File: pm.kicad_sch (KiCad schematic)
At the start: 15 parts, among them U10 INA237AIDGSR, U2 INA237AIDGSR, U6 INA237AIDGSR, U7 INA237AIDGSR, U9 INA237AIDGSR

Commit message: Added decouping caps
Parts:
- removed R25, R28, R29: 4.7K, symbol Device:R_US
- removed R26, R31, R32: SR: 0.001, symbol Device:R_US
- removed U10, U7, U9: INA237AIDGSR, VSSOP_IDGSR_TEX, symbol 2026-09-19_00-01-31:INA237AIDGSR
- added C40, C41: 0.1uF, symbol Device:C
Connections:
- net +3.3V: now also C40.1, C41.1
- net GND: now also C40.2, C41.2
- net +12V_B1 renamed +5.1V_UNFILT
- net +12V_B1_OUT renamed +5.1V
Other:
- note added: "5.1V Brick"
- note removed: "Brick 1"
- note removed: "Brick 2"
- note removed: "Brick 3"
- note removed: "Brick 4"
- note removed: "I2C Address: 0x42"
- note removed: "I2C Address: 0x43"
- note removed: "I2C Address: 0x44"

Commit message: Reverse polarity and power flow TBD, improved capacitance and labelling for nets
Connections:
- net +5.1V_UNFILT renamed +5.1V_RAW
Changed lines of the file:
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@@
 			)
 		)
-		(property "Value" "+5.1V_UNFILT"
+		(property "Value" "+5.1V_RAW"
 			(at 128.27 87.63 0)
 			(show_name no)

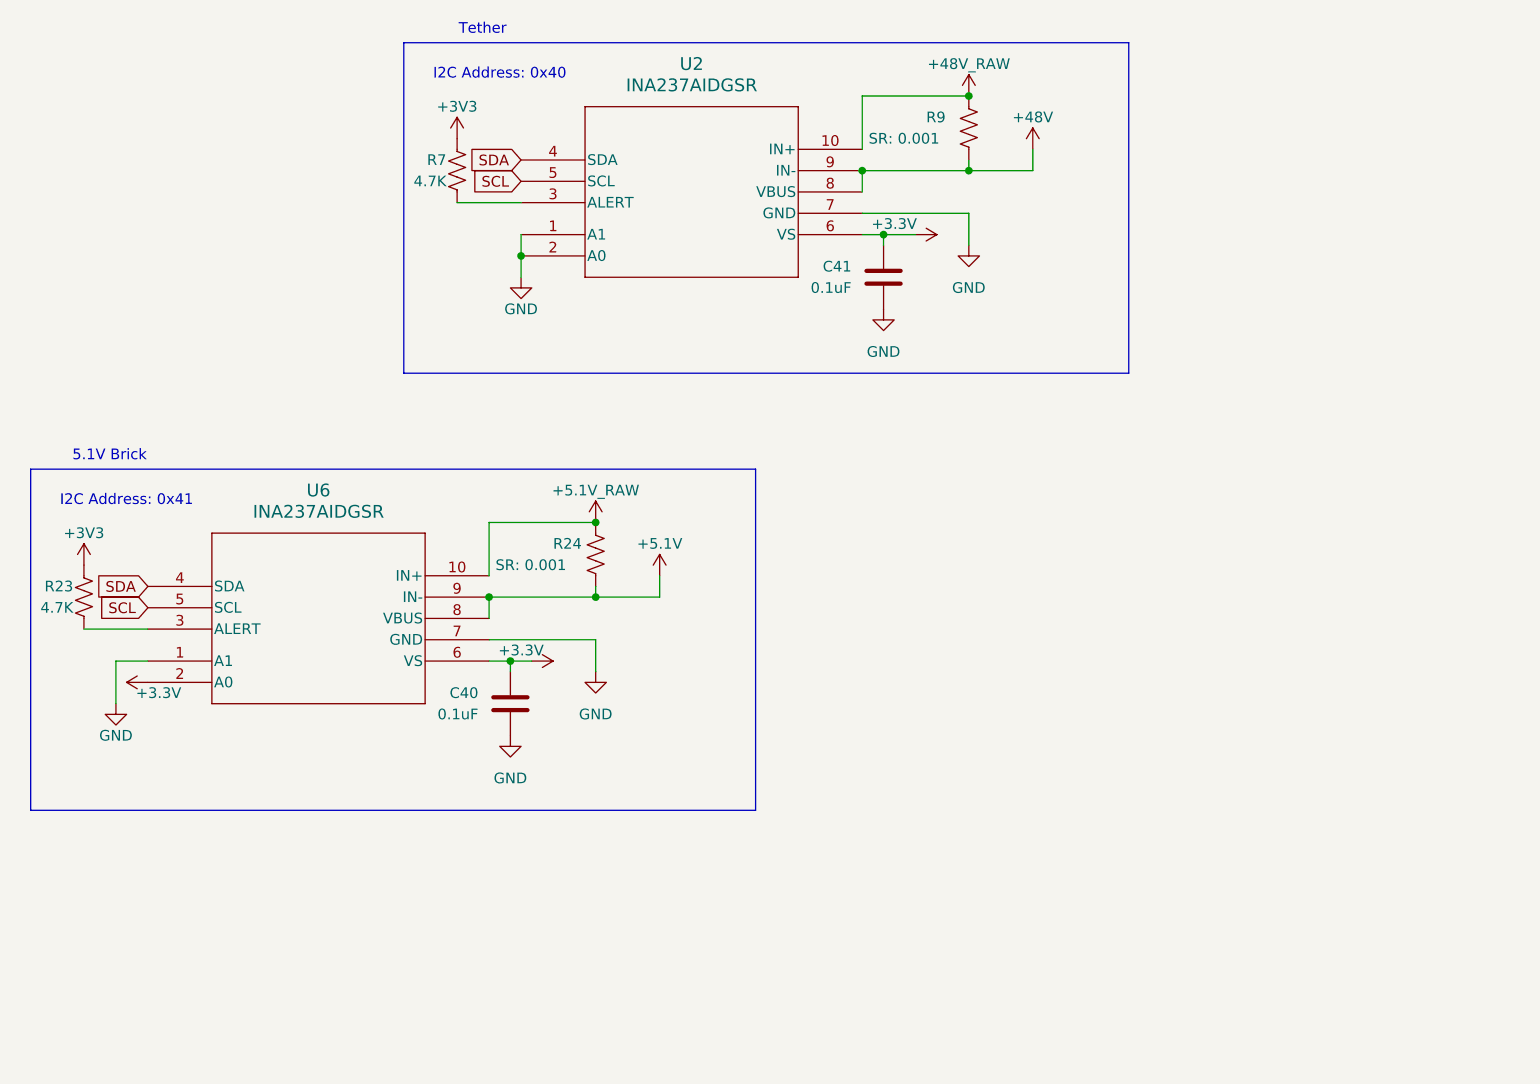
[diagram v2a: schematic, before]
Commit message: Prettified, more power changes and MCU pin changes and removing redundancies
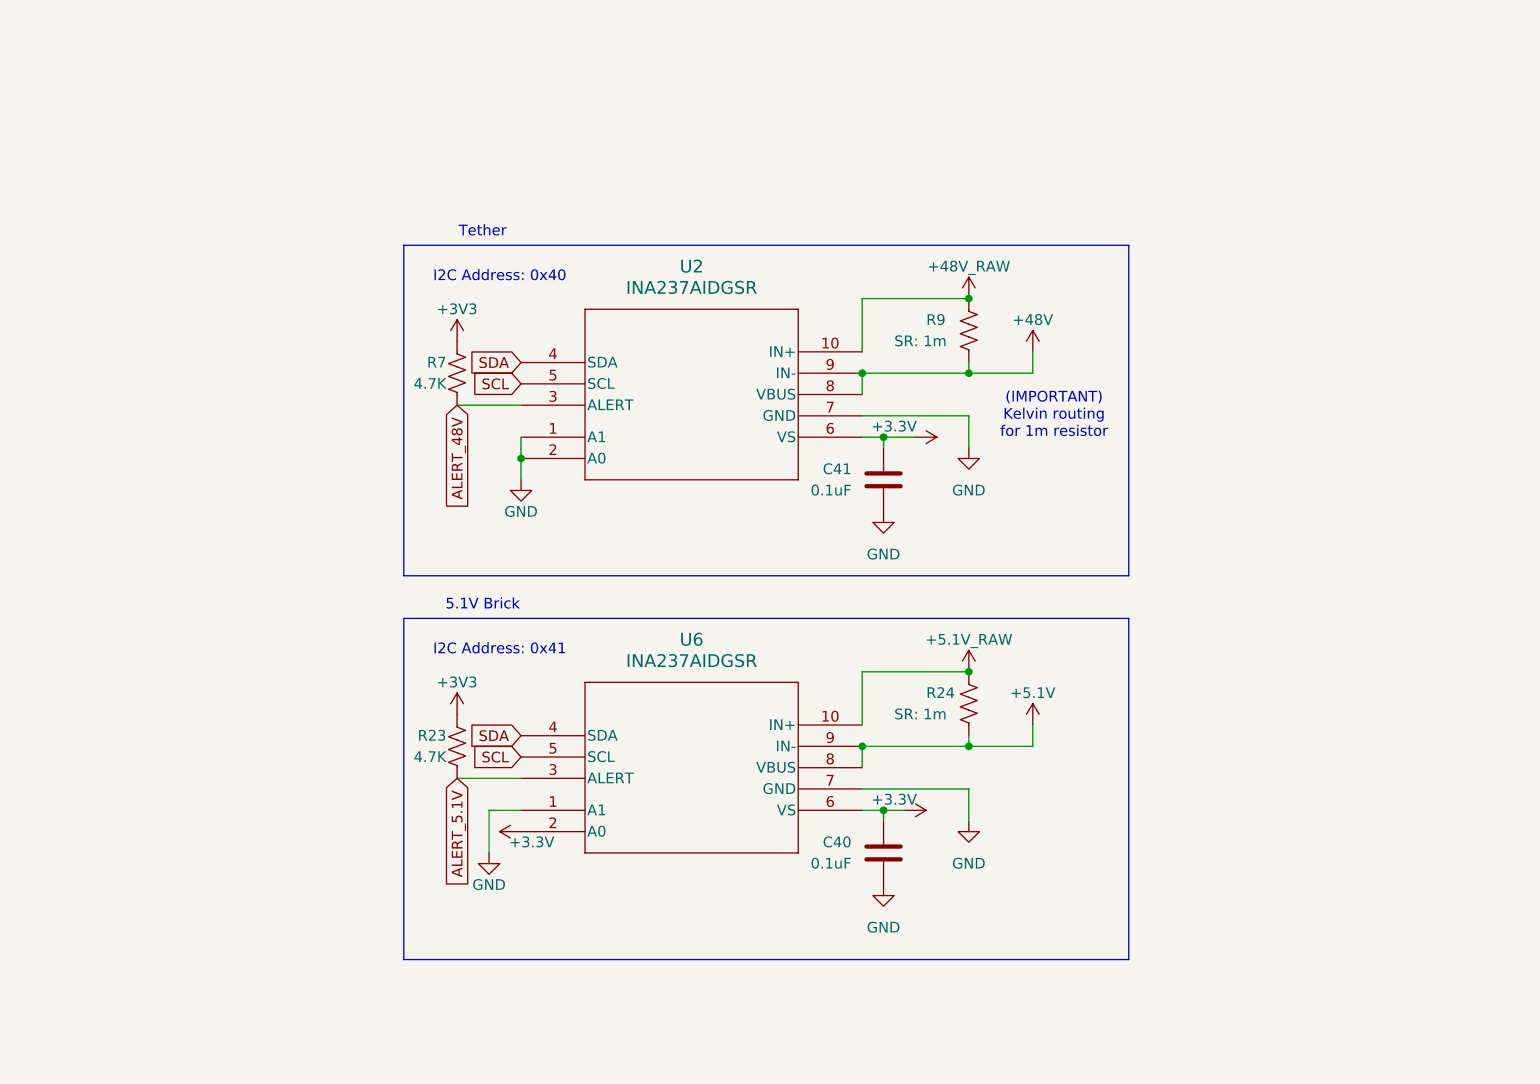
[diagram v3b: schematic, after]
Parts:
- R24, R9: value SR: 0.001 -> SR: 1m
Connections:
- net ALERT_5.1V: now reaches R23.2, U6.3 (ALERT)
- net ALERT_48V: now reaches R7.2, U2.3 (ALERT)
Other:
- note added: "(IMPORTANT) Kelvin routing for 1m resistor"
- moved on the sheet: C40, C41, R23, R24, R7, R9, U2, U6

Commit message: Replaced improper brick with new one
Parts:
- renumbered C41 to C42, C40 to C43, R7 to R21, R23 to R22, R9 to R23, U2 to U5
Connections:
- net ALERT_48V renamed INA_48V_ALERT_N
- net ALERT_5.1V renamed INA_5V1_ALERT_N
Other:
- note added: "(CHECKED)"
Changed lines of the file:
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@@
+		)
+	)
+	(text "(CHECKED)"
+		(exclude_from_sim no)
+		(at 125.73 101.6 0)
+		(effects
+			(font
+				(size 1.27 1.27)
+				(thickness 0.254)
+				(bold yes)
+				(color 224 48 15 1)
+			)
 		)
 	)
@@
 		)
 	)
+	(text "(CHECKED)"
+		(exclude_from_sim no)
+		(at 115.57 54.61 0)
+		(effects
+			(font
+				(size 1.27 1.27)
+				(thickness 0.254)
+				(bold yes)
+				(color 224 48 15 1)
+			)
+		)
+	)
 	(junction
 		(at 119.38 83.82)
@@
 		)
 	)
-	(global_label "ALERT_48V"
+	(global_label "INA_48V_ALERT_N"
 		(shape input)
 		(at 111.76 77.47 270)
@@
 		)
 		(property "Intersheetrefs" "${INTERSHEET_REFS}"
-			(at 111.76 90.4337 90)
+			(at 111.76 96.7233 90)
 			(hide yes)
 			(show_name no)
@@
 		)
 	)
-	(global_label "ALERT_5.1V"
+	(global_label "INA_5V1_ALERT_N"
 		(shape input)
 		(at 111.76 121.92 270)
@@
 		)
 		(property "Intersheetrefs" "${INTERSHEET_REFS}"
-			(at 111.76 135.4885 90)
+			(at 111.76 141.1733 90)
 			(hide yes)
 			(show_name no)
@@
 		(in_pos_files yes)
 		(dnp no)
-		(property "Reference" "R23"
+		(property "Reference" "R22"
 			(at 110.49 116.84 0)
 			(show_name no)
@@
 			(project "X19-Power-Slab-Board"
 				(path "/00000000-0000-0000-0000-000060e6118b/bbc862bf-048a-4900-acb1-a8352275c096"
-					(reference "R23")
+					(reference "R22")
 					(unit 1)
 				)
@@
 		(in_pos_files yes)
 		(dnp no)
-		(property "Reference" "#PWR032"
+		(property "Reference" "#PWR0105"
 			(at 119.38 92.71 0)
 			(hide yes)
@@
 			(project "X19-Power-Slab-Board"
 				(path "/00000000-0000-0000-0000-000060e6118b/bbc862bf-048a-4900-acb1-a8352275c096"
-					(reference "#PWR032")
+					(reference "#PWR0105")
 					(unit 1)
 				)
@@
 		(in_pos_files yes)
 		(dnp no)
-		(property "Reference" "#PWR0109"
+		(property "Reference" "#PWR0106"
 			(at 123.19 128.27 0)
 			(hide yes)
@@
 			(project "X19-Power-Slab-Board"
 				(path "/00000000-0000-0000-0000-000060e6118b/bbc862bf-048a-4900-acb1-a8352275c096"
-					(reference "#PWR0109")
+					(reference "#PWR0106")
 					(unit 1)
 				)
@@
 		(in_pos_files yes)
 		(dnp no)
-		(property "Reference" "R7"
+		(property "Reference" "R21"
 			(at 110.49 72.39 0)
 			(show_name no)
@@
 			(project "X19-Power-Slab-Board"
 				(path "/00000000-0000-0000-0000-000060e6118b/bbc862bf-048a-4900-acb1-a8352275c096"
-					(reference "R7")
+					(reference "R21")
 					(unit 1)
 				)
@@
 		(in_pos_files yes)
 		(dnp no)
-		(property "Reference" "#PWR095"
+		(property "Reference" "#PWR0104"
 			(at 115.57 137.16 0)
 			(hide yes)
@@
 			(project "X19-Power-Slab-Board"
 				(path "/00000000-0000-0000-0000-000060e6118b/bbc862bf-048a-4900-acb1-a8352275c096"
-					(reference "#PWR095")
+					(reference "#PWR0104")
 					(unit 1)
 				)
@@
 		(dnp no)
 		(fields_autoplaced yes)
-		(property "Reference" "#PWR0101"
+		(property "Reference" "#PWR0108"
 			(at 162.56 140.97 0)
 			(hide yes)
@@
 			(project "X19-Power-Slab-Board"
 				(path "/00000000-0000-0000-0000-000060e6118b/bbc862bf-048a-4900-acb1-a8352275c096"
-					(reference "#PWR0101")
+					(reference "#PWR0108")
 					(unit 1)
 				)
@@
 		(in_pos_files yes)
 		(dnp no)
-		(property "Reference" "C40"
+		(property "Reference" "C43"
 			(at 158.75 129.5399 0)
 			(show_name no)
@@
 			(project "X19-Power-Slab-Board"
 				(path "/00000000-0000-0000-0000-000060e6118b/bbc862bf-048a-4900-acb1-a8352275c096"
-					(reference "C40")
+					(reference "C43")
 					(unit 1)
 				)
@@
 		(dnp no)
 		(fields_autoplaced yes)
-		(property "Reference" "U2"
+		(property "Reference" "U5"
 			(at 139.7 60.96 0)
 			(show_name no)
@@
 			(project "X19-Power-Slab-Board"
 				(path "/00000000-0000-0000-0000-000060e6118b/bbc862bf-048a-4900-acb1-a8352275c096"
-					(reference "U2")
+					(reference "U5")
 					(unit 1)
 				)
@@
 		(in_pos_files yes)
 		(dnp no)
-		(property "Reference" "#PWR038"
+		(property "Reference" "#PWR0111"
 			(at 172.72 68.58 0)
 			(hide yes)
@@
 			(project "X19-Power-Slab-Board"
 				(path "/00000000-0000-0000-0000-000060e6118b/bbc862bf-048a-4900-acb1-a8352275c096"
-					(reference "#PWR038")
+					(reference "#PWR0111")
 					(unit 1)
 				)
@@
 		(in_pos_files yes)
 		(dnp no)
-		(property "Reference" "C41"
+		(property "Reference" "C42"
 			(at 158.75 85.0899 0)
 			(show_name no)
@@
 			(project "X19-Power-Slab-Board"
 				(path "/00000000-0000-0000-0000-000060e6118b/bbc862bf-048a-4900-acb1-a8352275c096"
-					(reference "C41")
+					(reference "C42")
 					(unit 1)
 				)
@@
 		(in_pos_files yes)
 		(dnp no)
-		(property "Reference" "#PWR094"
+		(property "Reference" "#PWR0103"
 			(at 111.76 118.11 0)
 			(hide yes)
@@
 			(project "X19-Power-Slab-Board"
 				(path "/00000000-0000-0000-0000-000060e6118b/bbc862bf-048a-4900-acb1-a8352275c096"
-					(reference "#PWR094")
+					(reference "#PWR0103")
 					(unit 1)
 				)
@@
 		(dnp no)
 		(fields_autoplaced yes)
-		(property "Reference" "#PWR098"
+		(property "Reference" "#PWR0114"
 			(at 172.72 133.35 0)
 			(hide yes)
@@
 			(project "X19-Power-Slab-Board"
 				(path "/00000000-0000-0000-0000-000060e6118b/bbc862bf-048a-4900-acb1-a8352275c096"
-					(reference "#PWR098")
+					(reference "#PWR0114")
 					(unit 1)
 				)
@@
 		(in_pos_files yes)
 		(dnp no)
-		(property "Reference" "#PWR040"
+		(property "Reference" "#PWR0115"
 			(at 180.34 74.93 0)
 			(hide yes)
@@
 			(project "X19-Power-Slab-Board"
 				(path "/00000000-0000-0000-0000-000060e6118b/bbc862bf-048a-4900-acb1-a8352275c096"
-					(reference "#PWR040")
+					(reference "#PWR0115")
 					(unit 1)
 				)
@@
 		(in_pos_files yes)
 		(dnp no)
-		(property "Reference" "R9"
+		(property "Reference" "R23"
 			(at 167.64 67.31 0)
 			(show_name no)
@@
 			(project "X19-Power-Slab-Board"
 				(path "/00000000-0000-0000-0000-000060e6118b/bbc862bf-048a-4900-acb1-a8352275c096"
-					(reference "R9")
+					(reference "R23")
 					(unit 1)
 				)
@@
 		(in_pos_files yes)
 		(dnp no)
-		(property "Reference" "#PWR099"
+		(property "Reference" "#PWR0116"
 			(at 180.34 119.38 0)
 			(hide yes)
@@
 			(project "X19-Power-Slab-Board"
 				(path "/00000000-0000-0000-0000-000060e6118b/bbc862bf-048a-4900-acb1-a8352275c096"
-					(reference "#PWR099")
+					(reference "#PWR0116")
 					(unit 1)
 				)
@@
 		(in_pos_files yes)
 		(dnp no)
-		(property "Reference" "#PWR035"
+		(property "Reference" "#PWR0110"
 			(at 162.56 81.28 0)
 			(hide yes)
@@
 			(project "X19-Power-Slab-Board"
 				(path "/00000000-0000-0000-0000-000060e6118b/bbc862bf-048a-4900-acb1-a8352275c096"
-					(reference "#PWR035")
+					(reference "#PWR0110")
 					(unit 1)
 				)
@@
 		(in_pos_files yes)
 		(dnp no)
-		(property "Reference" "#PWR097"
+		(property "Reference" "#PWR0113"
 			(at 172.72 113.03 0)
 			(hide yes)
@@
 			(project "X19-Power-Slab-Board"
 				(path "/00000000-0000-0000-0000-000060e6118b/bbc862bf-048a-4900-acb1-a8352275c096"
-					(reference "#PWR097")
+					(reference "#PWR0113")
 					(unit 1)
 				)
@@
 		(in_pos_files yes)
 		(dnp no)
-		(property "Reference" "#PWR031"
+		(property "Reference" "#PWR0102"
 			(at 111.76 73.66 0)
 			(hide yes)
@@
 			(project "X19-Power-Slab-Board"
 				(path "/00000000-0000-0000-0000-000060e6118b/bbc862bf-048a-4900-acb1-a8352275c096"
-					(reference "#PWR031")
+					(reference "#PWR0102")
 					(unit 1)
 				)
@@
 		(in_pos_files yes)
 		(dnp no)
-		(property "Reference" "#PWR096"
+		(property "Reference" "#PWR0109"
 			(at 161.29 125.73 0)
 			(hide yes)
@@
 			(project "X19-Power-Slab-Board"
 				(path "/00000000-0000-0000-0000-000060e6118b/bbc862bf-048a-4900-acb1-a8352275c096"
-					(reference "#PWR096")
+					(reference "#PWR0109")
 					(unit 1)
 				)
@@
 		(dnp no)
 		(fields_autoplaced yes)
-		(property "Reference" "#PWR039"
+		(property "Reference" "#PWR0112"
 			(at 172.72 88.9 0)
 			(hide yes)
@@
 			(project "X19-Power-Slab-Board"
 				(path "/00000000-0000-0000-0000-000060e6118b/bbc862bf-048a-4900-acb1-a8352275c096"
-					(reference "#PWR039")
+					(reference "#PWR0112")
 					(unit 1)
 				)
@@
 		(dnp no)
 		(fields_autoplaced yes)
-		(property "Reference" "#PWR0102"
+		(property "Reference" "#PWR0107"
 			(at 162.56 96.52 0)
 			(hide yes)
@@
 			(project "X19-Power-Slab-Board"
 				(path "/00000000-0000-0000-0000-000060e6118b/bbc862bf-048a-4900-acb1-a8352275c096"
-					(reference "#PWR0102")
+					(reference "#PWR0107")
 					(unit 1)
 				)

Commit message: updated some of nicks requested changes
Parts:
- U5, U6: footprint VSSOP_IDGSR_TEX -> rov_sensors:VSSOP_IDGSR_TEX
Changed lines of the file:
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@@
 			)
 		)
-		(property "Footprint" "VSSOP_IDGSR_TEX"
+		(property "Footprint" "rov_sensors:VSSOP_IDGSR_TEX"
 			(at 119.38 115.57 0)
 			(hide yes)
@@
 			)
 		)
-		(property "Footprint" "VSSOP_IDGSR_TEX"
+		(property "Footprint" "rov_sensors:VSSOP_IDGSR_TEX"
 			(at 119.38 71.12 0)
 			(hide yes)

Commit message: assigned some cap and res footprints
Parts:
- C42, C43: footprint (none) -> Capacitor_SMD:C_0603_1608Metric_Pad1.08x0.95mm_HandSolder
- R21, R22: footprint (none) -> Resistor_SMD:R_0603_1608Metric_Pad0.98x0.95mm_HandSolder
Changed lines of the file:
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@@
 			)
 		)
-		(property "Footprint" ""
+		(property "Footprint" "Resistor_SMD:R_0603_1608Metric_Pad0.98x0.95mm_HandSolder"
 			(at 112.776 118.364 90)
 			(hide yes)
@@
 			)
 		)
-		(property "Footprint" ""
+		(property "Footprint" "Resistor_SMD:R_0603_1608Metric_Pad0.98x0.95mm_HandSolder"
 			(at 112.776 73.914 90)
 			(hide yes)
@@
 			)
 		)
-		(property "Footprint" ""
+		(property "Footprint" "Capacitor_SMD:C_0603_1608Metric_Pad1.08x0.95mm_HandSolder"
 			(at 161.5948 134.62 0)
 			(hide yes)
@@
 			)
 		)
-		(property "Footprint" ""
+		(property "Footprint" "Capacitor_SMD:C_0603_1608Metric_Pad1.08x0.95mm_HandSolder"
 			(at 161.5948 90.17 0)
 			(hide yes)

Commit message: office hour changes
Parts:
- R23, R24: footprint (none) -> Resistor_SMD:R_2512_6332Metric_Pad1.40x3.35mm_HandSolder
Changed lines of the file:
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@@
 			)
 		)
-		(property "Footprint" ""
+		(property "Footprint" "Resistor_SMD:R_2512_6332Metric_Pad1.40x3.35mm_HandSolder"
 			(at 173.736 68.834 90)
 			(hide yes)
@@
 			)
 		)
-		(property "Footprint" ""
+		(property "Footprint" "Resistor_SMD:R_2512_6332Metric_Pad1.40x3.35mm_HandSolder"
 			(at 173.736 113.284 90)
 			(hide yes)
